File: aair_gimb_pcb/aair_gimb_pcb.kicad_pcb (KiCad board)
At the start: 2 copper layers, 71 parts, among them J3 USB_B_Mini, J4 SWD, Q1 sir182dp, Q2 sir182dp, Q3 sir182dp, Q4 sir182dp, Q5 sir182dp, Q6 sir182dp, U1 DRV8302, U2 STM32F405RGTx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

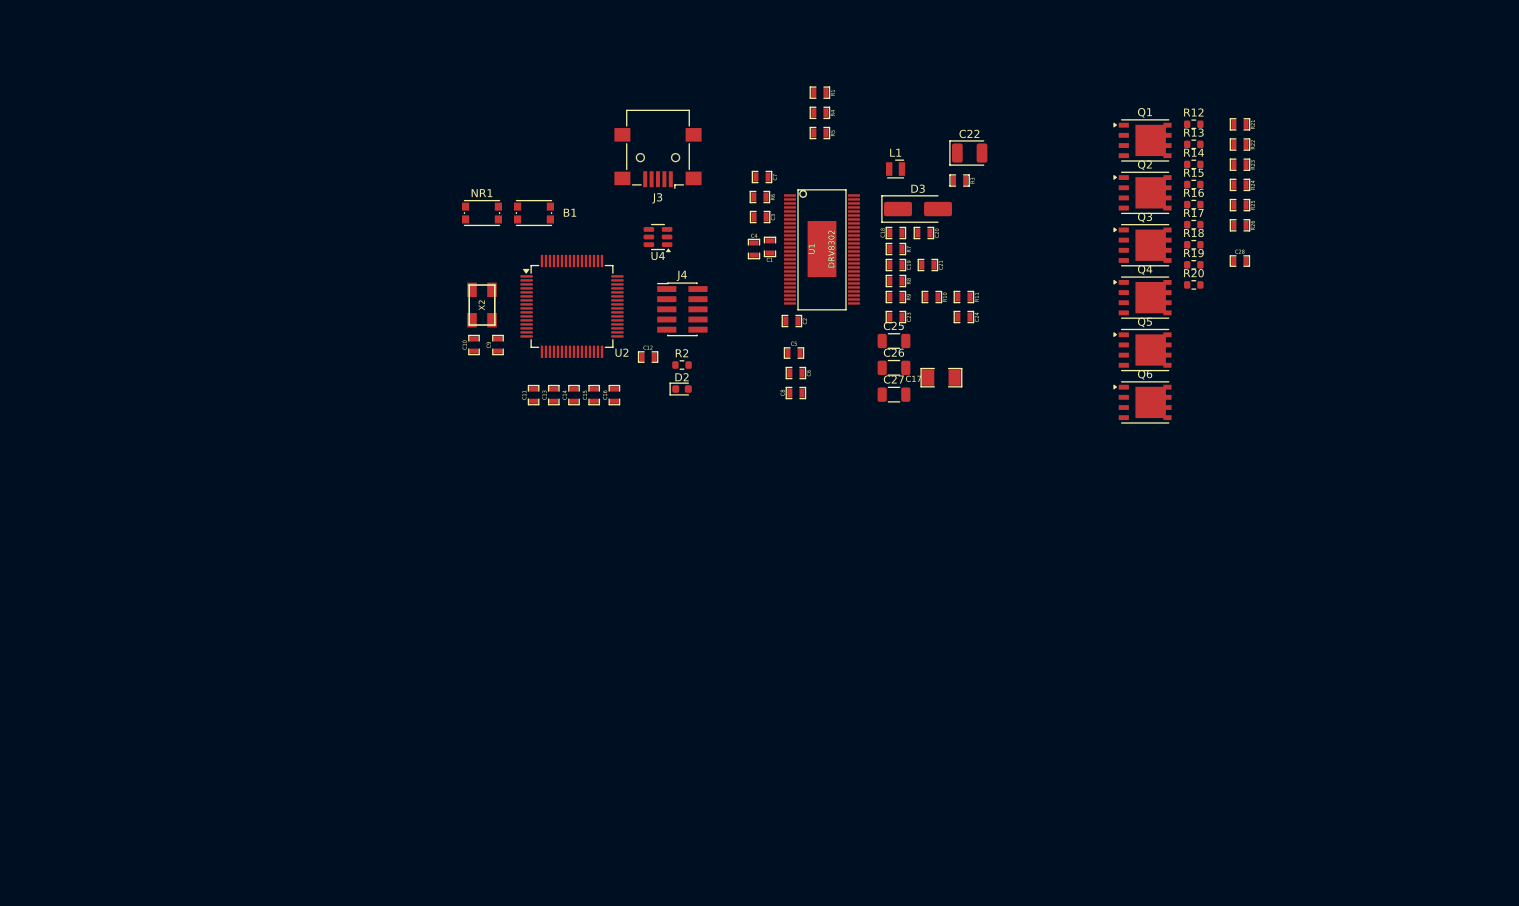
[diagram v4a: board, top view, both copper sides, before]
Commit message: сделать коннектор для переыерии
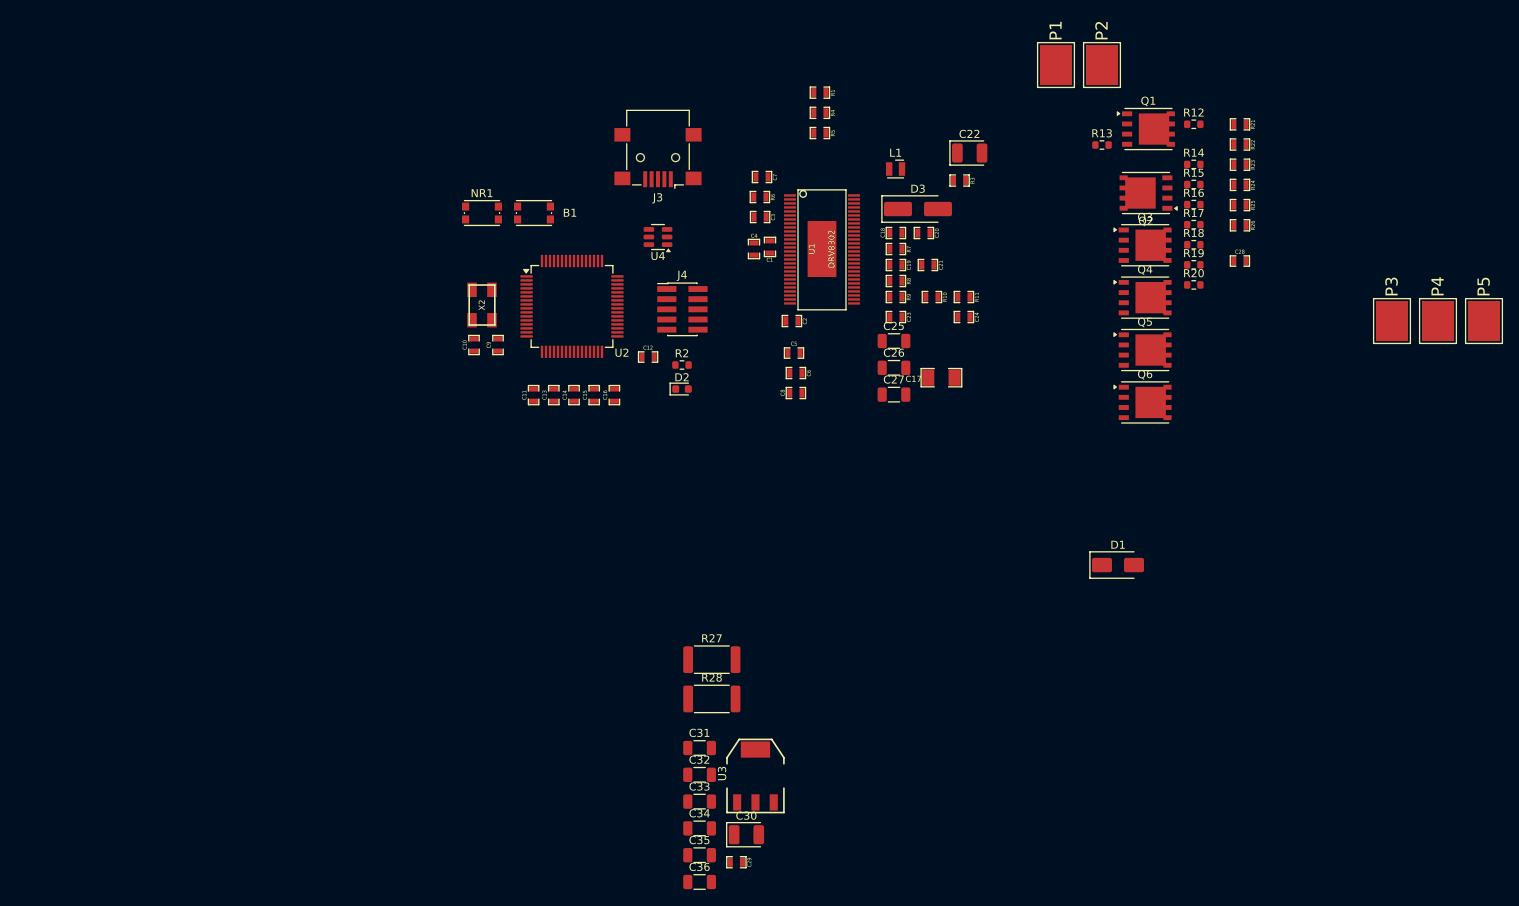
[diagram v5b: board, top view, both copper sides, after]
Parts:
- added C29: 2.2u, CRF1:SMD-0603_r, F.Cu at (156.8, 157.6)
- added C30: 100u, Capacitor_Tantalum_SMD:CP_EIA-3528-21_Kemet-B, F.Cu at (158.1, 154.2)
- added C31: 10u,50v, Capacitor_SMD:C_1206_3216Metric, F.Cu at (152.2, 143.4)
- added C32: 10u,50v, Capacitor_SMD:C_1206_3216Metric, F.Cu at (152.2, 146.7)
- added C33: 15u,50v, Capacitor_SMD:C_1206_3216Metric, F.Cu at (152.2, 150.1)
- added C34: 10u,50v, Capacitor_SMD:C_1206_3216Metric, F.Cu at (152.2, 153.4)
- added C35: 10u,50v, Capacitor_SMD:C_1206_3216Metric, F.Cu at (152.2, 156.8)
- added C36: 15u,50v, Capacitor_SMD:C_1206_3216Metric, F.Cu at (152.2, 160.1)
- added D1: TVS 5v, Diode_SMD:D_SMA, F.Cu at (204.5, 120.5)
- added P1: IN+, CRF1:1PAD_4x5mm, F.Cu at (196.8, 58.0)
- added P2: IN-, CRF1:1PAD_4x5mm, F.Cu at (202.5, 58.0)
- added P3: A, CRF1:1PAD_4x5mm, F.Cu at (238.8, 90.0)
- added P4: B, CRF1:1PAD_4x5mm, F.Cu at (244.5, 90.0)
- added P5: C, CRF1:1PAD_4x5mm, F.Cu at (250.2, 90.0)
- added R27: R005, Resistor_SMD:R_2512_6332Metric, F.Cu at (153.7, 132.3)
- added R28: R005, Resistor_SMD:R_2512_6332Metric, F.Cu at (153.7, 137.2)
- added U3: TC2117, CRF1:SOT-223, F.Cu at (159.2, 146.9)
- C22: value C_Polarized_Small_US -> 100u
- R2: value R_Small -> 220
- moved R13 11.5 mm to (202.5, 68.0)
- moved Q1 1.48 mm to (208.3, 66.0)
- moved Q2 0.11 mm to (208.0, 74.0), turned to 180 degrees
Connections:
- Q2 pad 1: /mosfet/H3_LOW -> V_SUPPLY
- Q2 pad 2: /mosfet/H3_LOW -> V_SUPPLY
- Q2 pad 3: /mosfet/H3_LOW -> V_SUPPLY
- Q4 pad 1: /mosfet/H2_LOW -> /drv8302/H2_LOW
- Q4 pad 2: /mosfet/H2_LOW -> /drv8302/H2_LOW
- Q4 pad 3: /mosfet/H2_LOW -> /drv8302/H2_LOW
- Q6 pad 1: /mosfet/H1_LOW -> /drv8302/H1_LOW
- Q6 pad 2: /mosfet/H1_LOW -> /drv8302/H1_LOW
- Q6 pad 3: /mosfet/H1_LOW -> /drv8302/H1_LOW
- R10 pad 2: /drv8302/SH2_A -> /drv8302/H2_LOW
- R11 pad 2: /drv8302/SH2_B -> V_SUPPLY
- R18 pad 2: /mosfet/H2_LOW -> /drv8302/H2_LOW
- R19 pad 2: /mosfet/H3_LOW -> V_SUPPLY
- R20 pad 2: /mosfet/H1_LOW -> /drv8302/H1_LOW
- R21 pad 1: Net-(R21-Pad1) -> /Stm32f405/SENS1
- R22 pad 1: Net-(R22-Pad1) -> /Stm32f405/SENS2
- R23 pad 1: Net-(R23-Pad1) -> /Stm32f405/SENS3
- R24 pad 1: Net-(R21-Pad1) -> /Stm32f405/SENS1
- R25 pad 1: Net-(R22-Pad1) -> /Stm32f405/SENS2
- R26 pad 1: Net-(R23-Pad1) -> /Stm32f405/SENS3
- R8 pad 2: /drv8302/SH1_A -> /drv8302/H1_LOW
- R9 pad 2: /drv8302/SH1_B -> V_SUPPLY
- U1 pad 10: /drv8302/GAIN -> /Stm32f405/GAIN
- U1 pad 12: /drv8302/DC_CAL -> /Stm32f405/DC_CAL
- U1 pad 16: /drv8302/EN_GATE -> /Stm32f405/EN_GATE
- U1 pad 25: /drv8302/Current_ADC_1 -> /Stm32f405/Current_ADC_1
- U1 pad 26: /drv8302/Current_ADC_2 -> /Stm32f405/Current_ADC_2
- U1 pad 34: /drv8302/H3_LOW -> V_SUPPLY
- U1 pad 6: /drv8302/FAULT -> /Stm32f405/FAULT
- U1 pad 8: /drv8302/M_PWM -> /Stm32f405/M_PWM
- U2 pad 10: LED_STATUS -> /Stm32f405/SENS3
- U2 pad 11: unconnected-(U2-PC3-Pad11) -> LED_STATUS
- U2 pad 14: unconnected-(U2-PA0-Pad14) -> /Stm32f405/Current_ADC_1
- U2 pad 15: unconnected-(U2-PA1-Pad15) -> /Stm32f405/Current_ADC_2
- U2 pad 16: unconnected-(U2-PA2-Pad16) -> ADC3
- U2 pad 17: unconnected-(U2-PA3-Pad17) -> /Stm32f405/EN_GATE
- U2 pad 20: unconnected-(U2-PA4-Pad20) -> SPI1_CS
- U2 pad 21: unconnected-(U2-PA5-Pad21) -> SPI1_SCK
- U2 pad 22: unconnected-(U2-PA6-Pad22) -> SPI1_MISO
- U2 pad 23: unconnected-(U2-PA7-Pad23) -> SPI1_MOSI
- U2 pad 26: unconnected-(U2-PB0-Pad26) -> /Stm32f405/M_PWM
- U2 pad 27: unconnected-(U2-PB1-Pad27) -> /Stm32f405/GAIN
- U2 pad 29: unconnected-(U2-PB10-Pad29) -> /Stm32f405/FAULT
- U2 pad 30: unconnected-(U2-PB11-Pad30) -> /Stm32f405/DC_CAL
- U2 pad 34: /Stm32f405/L3 -> /Stm32f405/L1
- U2 pad 36: /Stm32f405/L1 -> /Stm32f405/L3
- U2 pad 51: unconnected-(U2-PC10-Pad51) -> UART_TX
- U2 pad 52: unconnected-(U2-PC11-Pad52) -> UART_RX
- U2 pad 59: unconnected-(U2-PB7-Pad59) -> I2C_SDA
- U2 pad 61: unconnected-(U2-PB8-Pad61) -> I2C_SCL
- U2 pad 8: unconnected-(U2-PC0-Pad8) -> /Stm32f405/SENS1
- U2 pad 9: unconnected-(U2-PC1-Pad9) -> /Stm32f405/SENS2

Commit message: pcb
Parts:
- added J1: I2C, Connector_JST:JST_GH_BM04B-GHS-TBT_1x04-1MP_P1.25mm_Vertical, F.Cu at (138.1, 115.1)
- added J2: UART, Connector_JST:JST_GH_BM04B-GHS-TBT_1x04-1MP_P1.25mm_Vertical, F.Cu at (149.3, 115.1)
- added J6: SPI1, Connector_JST:JST_GH_BM06B-GHS-TBT_1x06-1MP_P1.25mm_Vertical, F.Cu at (126.5, 115.1)
- D3: footprint Diode_SMD:D_SMA_Handsoldering -> Diode_SMD:D_SMA
- L1: footprint Inductor_SMD_Wurth:L_Wurth_WE-LQSH-2010 -> Inductor_SMD:L_7.3x7.3_H4.5
- moved C29 93.8 mm to (161.2, 64.0), turned to 180 degrees
- moved C30 90.5 mm to (165.5, 64.0)
- moved U3 77.9 mm to (156.0, 69.0), turned to 90 degrees
- moved C31 72.8 mm to (106.4, 86.9)
- moved C32 72.8 mm to (106.4, 90.2)
- moved C35 72.8 mm to (106.4, 100.3)
- moved C36 72.8 mm to (106.4, 103.6)
- moved C33 72.8 mm to (106.4, 93.6)
- moved C34 72.8 mm to (106.4, 96.9)
- moved C1 62.1 mm to (109.3, 115.1)
- moved C3 62.1 mm to (108.1, 111.4)
- moved C4 62.1 mm to (107.3, 115.4)
- moved C7 62.1 mm to (108.3, 106.4)
- moved R6 62.1 mm to (108.1, 108.9)
- moved P2 61.0 mm to (182.1, 115.5), turned to 180 degrees
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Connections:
- B1 pad 1: V_SUPPLY -> GND
- C10 pad 2: V_SUPPLY -> GND
- C11 pad 1: V_SUPPLY -> GND
- C12 pad 1: V_SUPPLY -> GND
- C13 pad 1: V_SUPPLY -> GND
- C14 pad 1: V_SUPPLY -> GND
- C15 pad 1: V_SUPPLY -> GND
- C16 pad 1: V_SUPPLY -> GND
- C17 pad 1: V_SUPPLY -> GND
- C17 pad 2: Net-(C17-Pad2) -> V_SUPPLY
- C2 pad 2: V_SUPPLY -> GND
- C22 pad 2: V_SUPPLY -> GND
- C25 pad 1: V_SUPPLY -> GND
- C26 pad 1: V_SUPPLY -> GND
- C27 pad 1: V_SUPPLY -> GND
- C28 pad 1: V_SUPPLY -> GND
- C29 pad 2: V_SUPPLY -> GND
- C3 pad 2: V_SUPPLY -> GND
- C30 pad 2: V_SUPPLY -> GND
- C31 pad 2: V_SUPPLY -> GND
- C32 pad 2: V_SUPPLY -> GND
- C33 pad 2: V_SUPPLY -> GND
- C34 pad 2: V_SUPPLY -> GND
- C35 pad 2: V_SUPPLY -> GND
- C36 pad 2: V_SUPPLY -> GND
- C4 pad 2: V_SUPPLY -> GND
- C5 pad 2: V_SUPPLY -> GND
- C6 pad 2: V_SUPPLY -> GND
- C7 pad 1: V_SUPPLY -> GND
- C8 pad 1: V_SUPPLY -> GND
- C9 pad 2: V_SUPPLY -> GND
- D1 pad 2: V_SUPPLY -> GND
- D3 pad 2: V_SUPPLY -> GND
- J3 pad 5: V_SUPPLY -> GND
- J4 pad 3: V_SUPPLY -> GND
- J4 pad 5: V_SUPPLY -> GND
- J4 pad 9: V_SUPPLY -> GND
- NR1 pad 1: V_SUPPLY -> GND
- P2 pad 1: V_SUPPLY -> GND
- Q2 pad 1: V_SUPPLY -> GND
- Q2 pad 2: V_SUPPLY -> GND
- Q2 pad 3: V_SUPPLY -> GND
- R1 pad 1: V_SUPPLY -> GND
- R11 pad 2: V_SUPPLY -> GND
- R19 pad 2: V_SUPPLY -> GND
- R2 pad 2: V_SUPPLY -> GND
- R21 pad 2: unconnected-(R21-Pad2) -> /drv8302/H1_VS
- R22 pad 2: unconnected-(R22-Pad2) -> /drv8302/H2_VS
- R23 pad 2: unconnected-(R23-Pad2) -> /drv8302/H3_VS
- R24 pad 2: V_SUPPLY -> GND
- R25 pad 2: V_SUPPLY -> GND
- R26 pad 2: V_SUPPLY -> GND
- R27 pad 2: V_SUPPLY -> GND
- R28 pad 2: V_SUPPLY -> GND
- R3 pad 1: V_SUPPLY -> GND
- R6 pad 2: V_SUPPLY -> GND
- R7 pad 2: V_SUPPLY -> GND
- R9 pad 2: V_SUPPLY -> GND
- U1 pad 28: V_SUPPLY -> GND
- U1 pad 34: V_SUPPLY -> GND
- U1 pad 53: Net-(C17-Pad2) -> V_SUPPLY
- U1 pad 54: Net-(C17-Pad2) -> V_SUPPLY
- U1 pad 57: V_SUPPLY -> GND
- U2 pad 12: V_SUPPLY -> GND
- U2 pad 14: /Stm32f405/Current_ADC_1 -> ADC3
- U2 pad 16: ADC3 -> /Stm32f405/Current_ADC_1
- U2 pad 18: V_SUPPLY -> GND
- U2 pad 63: V_SUPPLY -> GND
- U3 pad 1: V_SUPPLY -> GND
- U4 pad 2: V_SUPPLY -> GND
- X2 pad 3: V_SUPPLY -> GND
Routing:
- net /drv8302/H3_VS: track 0.00 -> 66.0 mm
- net /drv8302/H2_VS: track 0.00 -> 51.4 mm
- net /drv8302/M_H1: track 0.00 -> 43.2 mm, vias 0 -> 2
- net /drv8302/M_L2: track 0.00 -> 41.3 mm, vias 0 -> 2
- net /drv8302/M_H3: track 0.00 -> 37.8 mm, vias 0 -> 2
- net /drv8302/M_H2: track 0.00 -> 37.7 mm, vias 0 -> 2
- net /drv8302/M_L3: track 0.00 -> 37.3 mm, vias 0 -> 2
- net /drv8302/M_L1: track 0.00 -> 28.3 mm, vias 0 -> 2
- net /Stm32f405/GAIN: track 0.00 -> 23.8 mm, vias 0 -> 2
- net /Stm32f405/EN_GATE: track 0.00 -> 21.9 mm, vias 0 -> 2
- net /Stm32f405/DC_CAL: track 0.00 -> 20.0 mm, vias 0 -> 2
- net /Stm32f405/Current_ADC_2: track 0.00 -> 19.5 mm, vias 0 -> 2
- net /Stm32f405/Current_ADC_1: track 0.00 -> 19.0 mm
- net GND: track 0.00 -> 17.0 mm
- net Net-(U1-SP2): track 0.00 -> 14.0 mm
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- added copper zone on F.Cu, net /drv8302/H3_VS

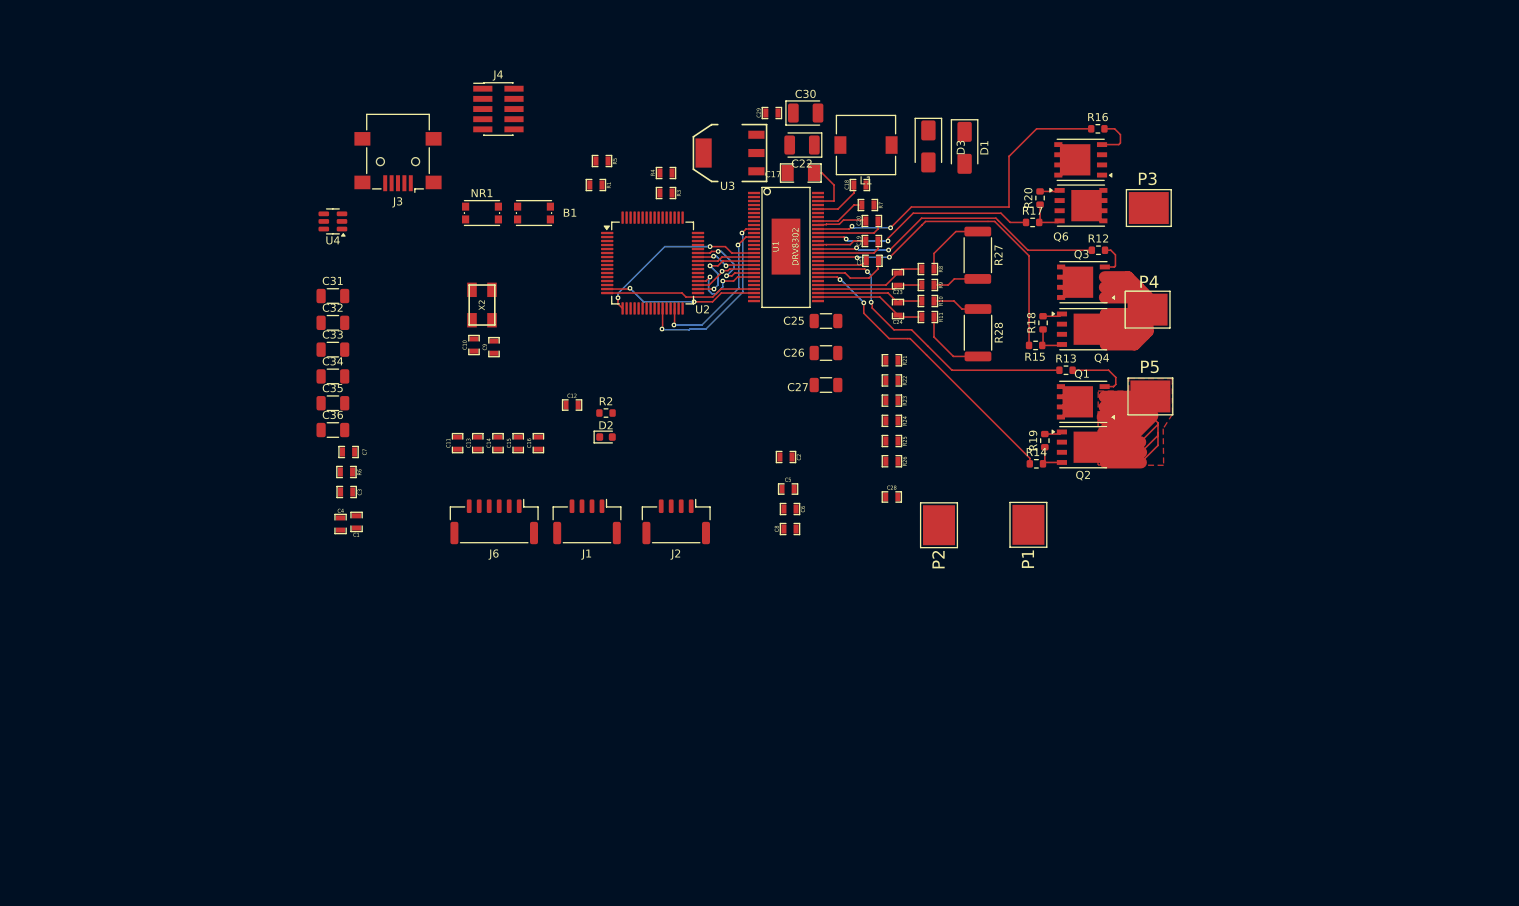
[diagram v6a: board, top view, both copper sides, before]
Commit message: add digital logic to pcb
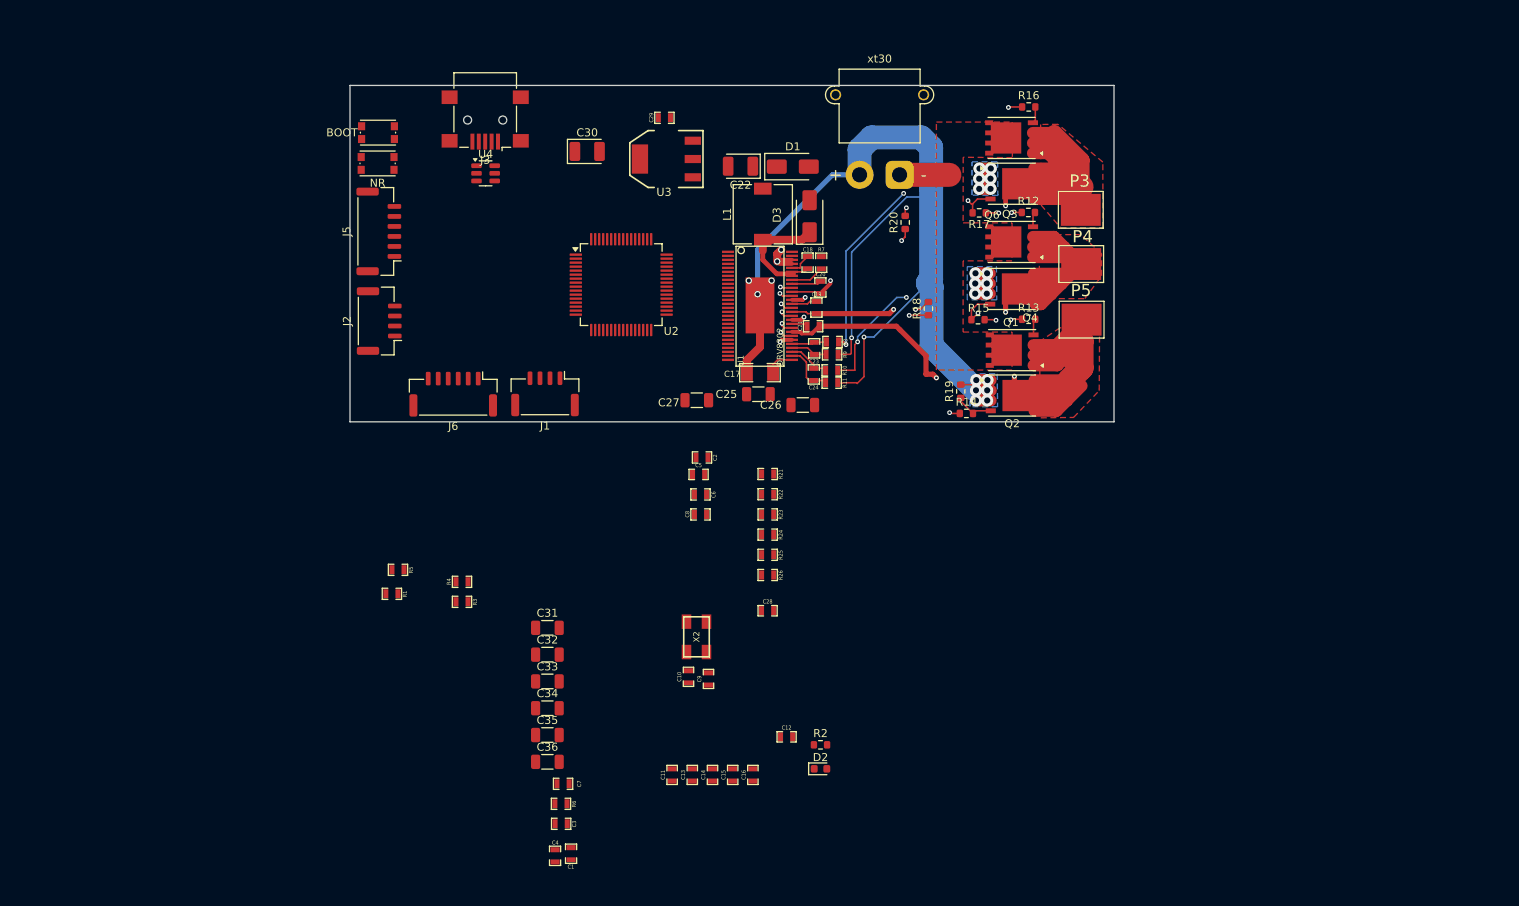
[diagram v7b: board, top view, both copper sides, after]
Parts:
- removed J4: SWD, Connector_PinHeader_1.27mm:PinHeader_2x05_P1.27mm_Vertical_SMD
- removed P1: IN+, CRF1:1PAD_4x5mm
- removed P2: IN-, CRF1:1PAD_4x5mm
- added J5: SWD, Connector_JST:JST_GH_BM06B-GHS-TBT_1x06-1MP_P1.25mm_Vertical, F.Cu at (112.1, 78.8)
- added xt30: XT30, Connector_AMASS:AMASS_XT30PW-M_1x02_P2.50mm_Horizontal, F.Cu at (177.2, 71.7)
- R27, R28: moved to B.Cu
- moved R1 57.1 mm to (113.7, 124.1)
- moved R3 57.1 mm to (122.5, 125.1)
- moved R4 57.1 mm to (122.5, 122.6)
- moved R5 57.1 mm to (114.5, 121.1)
- moved C33 49.4 mm to (133.2, 135.1)
- moved C34 49.4 mm to (133.2, 138.4)
- moved C1 49.4 mm to (136.1, 156.6)
- moved C3 49.4 mm to (134.9, 152.8)
- moved C4 49.4 mm to (134.1, 156.8)
- moved C7 49.4 mm to (135.1, 147.8)
- moved R6 49.4 mm to (134.9, 150.3)
- moved C31 49.4 mm to (133.2, 128.3)
- moved C32 49.4 mm to (133.2, 131.7)
- moved C35 49.4 mm to (133.2, 141.8)
- moved C36 49.4 mm to (133.2, 145.1)
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- renumbered B1 to BOOT, NR1 to NR
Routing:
- net GND: track 17.0 -> 139.9 mm, vias 0 -> 12
- net /drv8302/H1_VS: track 8.21 -> 86.1 mm, vias 0 -> 2
- net /drv8302/H1_LOW: track 11.1 -> 79.6 mm, vias 0 -> 10
- net /drv8302/H2_LOW: track 8.40 -> 65.2 mm, vias 0 -> 10
- net V_SUPPLY: track 7.12 -> 33.8 mm, vias 0 -> 2
- net /Stm32f405/GAIN: track 23.8 -> 0.00 mm, vias 2 -> 0
- net /Stm32f405/EN_GATE: track 21.9 -> 0.00 mm, vias 2 -> 0
- net /drv8302/H3_VS: track 66.0 -> 87.3 mm, vias 0 -> 2
- net /Stm32f405/DC_CAL: track 20.0 -> 0.00 mm, vias 2 -> 0
- net /Stm32f405/Current_ADC_2: track 19.5 -> 0.00 mm, vias 2 -> 0
- net /Stm32f405/Current_ADC_1: track 19.0 -> 0.00 mm
- net /drv8302/H2_VS: track 51.4 -> 69.3 mm, vias 0 -> 2
- net Net-(D3-K): track 0.00 -> 15.4 mm
- net Net-(Q4-G): track 4.56 -> 16.1 mm, vias 0 -> 2
- net Net-(Q6-G): track 4.90 -> 16.4 mm, vias 0 -> 2
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- added copper zone on B.Cu, net /drv8302/H1_LOW
- added copper zone on F.Cu, net /drv8302/H1_VS
- added copper zone on B.Cu, net /drv8302/H2_LOW
- added copper zone on F.Cu, net /drv8302/H2_VS
- added copper zone on B.Cu, net GND
- added copper zone on F.Cu, net V_SUPPLY
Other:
- board outline added: 95.5 x 42 mm
- copper layers 2 -> 4
- board text added: "BOOT"
